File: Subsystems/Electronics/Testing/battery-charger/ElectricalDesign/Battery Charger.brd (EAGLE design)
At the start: 100 x 80 mm, 117 parts, among them J1 USB4515-GF-A_REVA, J3 10103592-0001LF, Q1 CSD16406Q3, Q2 CSD16406Q3, Q3 DMN2008LFU, Q4 DMN2008LFU, Q5 DMN2008LFU, Q6 BC817, Q7 BC817, SW6 [Override], U1 BQ24650, U2 BQ29700, U3 BQ29700, U4 BQ29700, U5 CP2102N-A02-GQFN28, U7 ESP32-S2-MINI-1

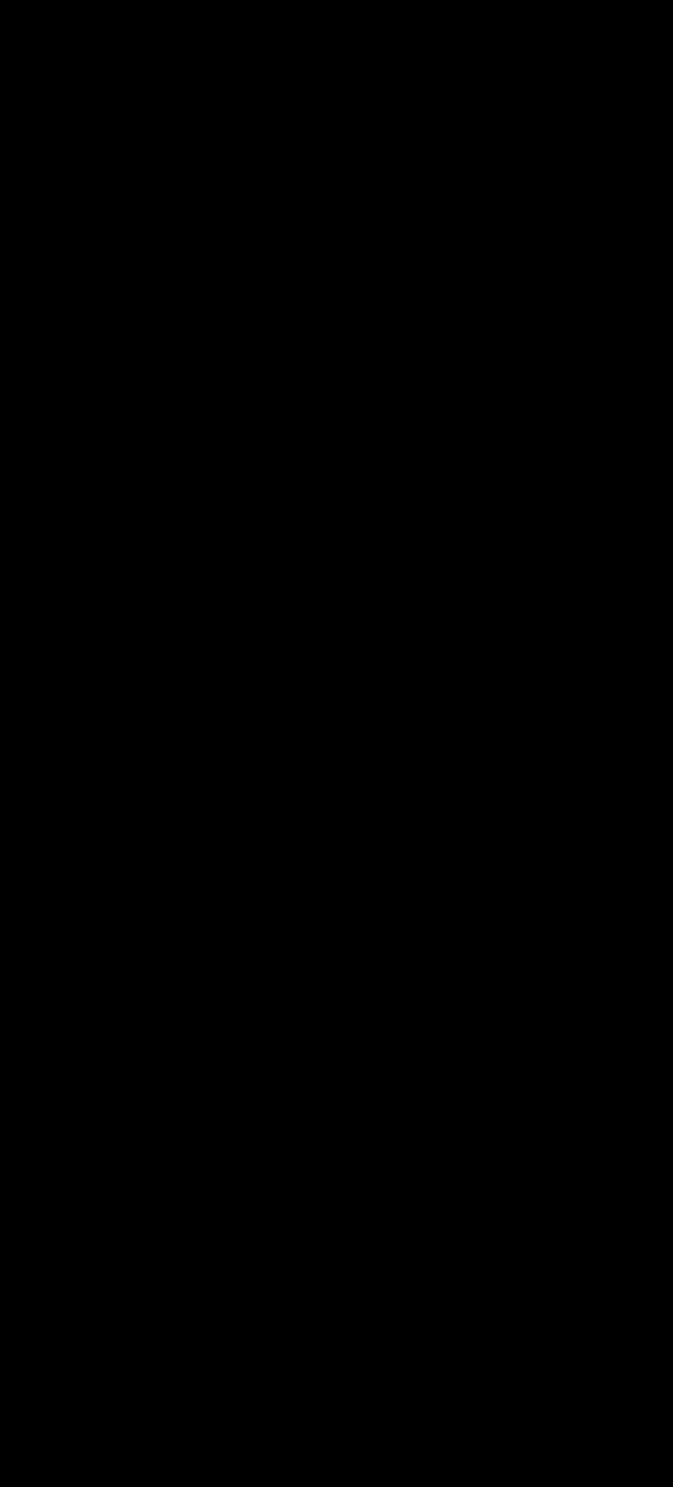
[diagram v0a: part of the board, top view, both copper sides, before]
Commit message: Added Test Points
Added test points for the important nets
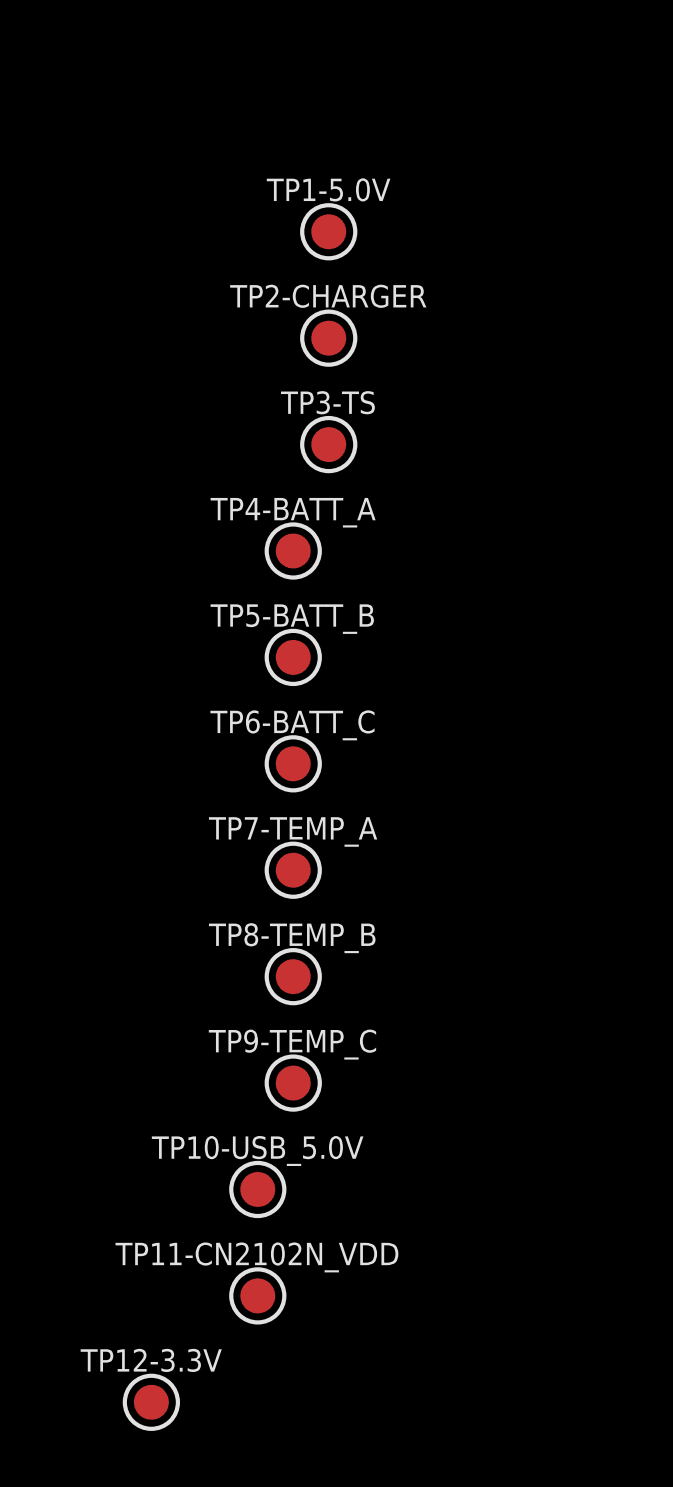
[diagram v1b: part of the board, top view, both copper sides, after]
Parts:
- added TP1-5.0V, TP10-USB_5.0V, TP11-CN2102N_VDD, TP12-3.3V, TP2-CHARGER, TP3-TS, TP4-BATT_A, TP5-BATT_B, TP6-BATT_C, TP7-TEMP_A, TP8-TEMP_B, TP9-TEMP_C: TEST_POINT-SMD-C-1.25, CougsInSpace-Connectors:SMD-C-1.25
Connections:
- removed net TEMP1: R38.1, RT1.2, U7.11
- removed net TEMP2: R39.1, RT2.2, U7.12
- removed net TEMP3: R40.1, RT3.2, U7.13
- new net TEMP_A: R38.1, RT1.2, TP7-TEMP_A.1, U7.11
- new net TEMP_B: R39.1, RT2.2, TP8-TEMP_B.1, U7.12
- new net TEMP_C: R40.1, RT3.2, TP9-TEMP_C.1, U7.13
- net 3.3V: now also TP12-3.3V.1
- net 5.0V: now also TP1-5.0V.1
- net CHARGER: now also TP2-CHARGER.1
- net CP2102N_VDD: now also TP11-CN2102N_VDD.1
- net D3_OUT: now also TP4-BATT_A.1
- net D4_OUT: now also TP5-BATT_B.1
- net D5_OUT: now also TP6-BATT_C.1
- net TS-ESP: now also TP3-TS.1
- net USB_VDD: now also TP10-USB_5.0V.1

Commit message: Completed Board Layout
Completed board layout, ready for review. Sense resistors were adjusted from 20m to 25m Ohm. Additional sense pins added.
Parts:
- added R42, R43: 0Ω <20mΩ, CougsInSpace-Resistors:1608
- added TP13-GND, TP14-D1_OUT: TEST_POINT-SMD-C-1.25, CougsInSpace-Connectors:SMD-C-1.25
- C20: value 10µF 10% -> 1µF 10%
- JP1: device pinhead:1X07 -> pinhead:1X11
- R18, R19: value 10mΩ 1% -> 50mΩ 1%; device CougsInSpace-Resistors:3216 -> CougsInSpace-Resistors:1608
- moved TP4-BATT_A 734.8 mm to (88.5, 70.5)
- moved TP7-TEMP_A 732.4 mm to (88.5, 56.5), turned to 180 degrees
- moved TP11-CN2102N_VDD 730.2 mm to (12.5, 61.5)
- moved TP12-3.3V 718.3 mm to (31.0, 39.5), turned to 90 degrees
- moved TP5-BATT_B 714.9 mm to (88.5, 45.5)
- moved TP10-USB_5.0V 713.4 mm to (10.5, 48.5), turned to 180 degrees
- moved TP8-TEMP_B 712.5 mm to (88.5, 31.5), turned to 180 degrees
- moved TP6-BATT_C 695.6 mm to (88.5, 21.0)
- moved TP9-TEMP_C 693.2 mm to (88.5, 7.00), turned to 180 degrees
- moved TP3-TS 686.4 mm to (53.5, 35.5)
- moved TP2-CHARGER 679.3 mm to (48.5, 33.5)
- moved TP1-5.0V 669.6 mm to (11.5, 38.0)
- moved R41 646.5 mm to (64.5, 50.5)
- moved C23 636.4 mm to (81.0, 65.0)
- moved C24 626.7 mm to (81.0, 40.0)
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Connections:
- removed net N$8: R18.2, R19.1
- new net CHASSIS: J1.S1, J1.S2, J1.S3, J1.S4, J3.S1, J3.S2, J3.S3, J3.S4, J3.S5, J3.S6, R43.1
- new net DGND: C25.2, C26.2, C27.2, C28.2, J3.5, R42.1, U5.29, U5.3
- net 3.3V: now also JP1.11
- net 5.0V: now also JP1.1
- net BQ24650_SR_P: now also R19.1
- net CHARGER: now also R18.2
- net D1_OUT: now also TP14-D1_OUT.1
- net ESP32_IO12: now also JP1.9; no longer JP1.7
- net ESP32_IO13: now also JP1.8; no longer JP1.6
- net ESP32_IO14: now also JP1.7; no longer JP1.5
- net ESP32_IO15: now also JP1.6; no longer JP1.4
- net ESP32_IO16: now also JP1.5; no longer JP1.3
- net ESP32_IO17: now also JP1.4; no longer JP1.2
- net ESP32_IO18: now also JP1.3; no longer JP1.1
- net PGND: now also JP1.10, JP1.2, R42.2, R43.2, TP13-GND.1; no longer C25.2, C26.2, C27.2, C28.2, J1.S1, J1.S2, J1.S3, J1.S4, J3.5, J3.S1, J3.S2, J3.S3, J3.S4, J3.S5, J3.S6, U5.29, U5.3
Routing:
- net PGND: track 0.00 -> 771.8 mm, vias 0 -> 22
- net 5.0V: track 0.00 -> 315.4 mm, vias 0 -> 11
- net TEMP_C: track 0.00 -> 114.5 mm, vias 0 -> 3
- net TEMP_B: track 0.00 -> 95.3 mm, vias 0 -> 3
- net TEMP_A: track 0.00 -> 93.7 mm, vias 0 -> 3
- net BQ297002_VSS: track 0.00 -> 91.6 mm
- net BQ297001_VSS: track 0.00 -> 91.6 mm
- net BQ297003_VSS: track 0.00 -> 91.3 mm
- net CHARGER: track 0.00 -> 81.0 mm
- net 3.3V: track 0.00 -> 75.5 mm, vias 0 -> 2
- net STAT3: track 0.00 -> 65.2 mm, vias 0 -> 3
- net STAT2: track 0.00 -> 60.5 mm, vias 0 -> 3
- net SW3: track 0.00 -> 54.8 mm, vias 0 -> 1
- net CHASSIS: track 0.00 -> 50.8 mm
- net D3_OUT: track 0.00 -> 50.3 mm
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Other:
- board size 100 x 80 mm -> 165 x 75 mm
- board text added: "12"
- board text added: "13"
- board text added: "14"
- board text added: "15"
- board text added: "16"
- board text added: "17"
- board text added: "18"
- board text added: "19"
- board text added: "20"
- board text added: "21"
- board text added: "26"
- board text added: "33"
- board text added: "34"
- board text added: "35"
- board text added: "36"
- board text added: "37"
- board text added: "38"
- board text added: "39"
- board text added: "3V3"
- board text added: "40"
- board text added: "41"
- board text added: "42"
- board text added: "45"
- board text added: "46"
- board text added: "5V"
- board text added: "Battery Charger V1.0.0"
- board text added: "Charging"
- board text added: "Complete"
- board text added: "GND"
- board text added: "Power"
- board text added: "Prog Data"
- board text added: "RESET"
- board text added: "TP1"
- board text added: "TP10"
- board text added: "TP11"
- board text added: "TP12"
- board text added: "TP13"
- board text added: "TP14"
- board text added: "TP2"
- board text added: "TP3"
- board text added: "TP4"
- board text added: "TP5"
- board text added: "TP6"
- board text added: "TP7"
- board text added: "TP8"
- board text added: "TP9"

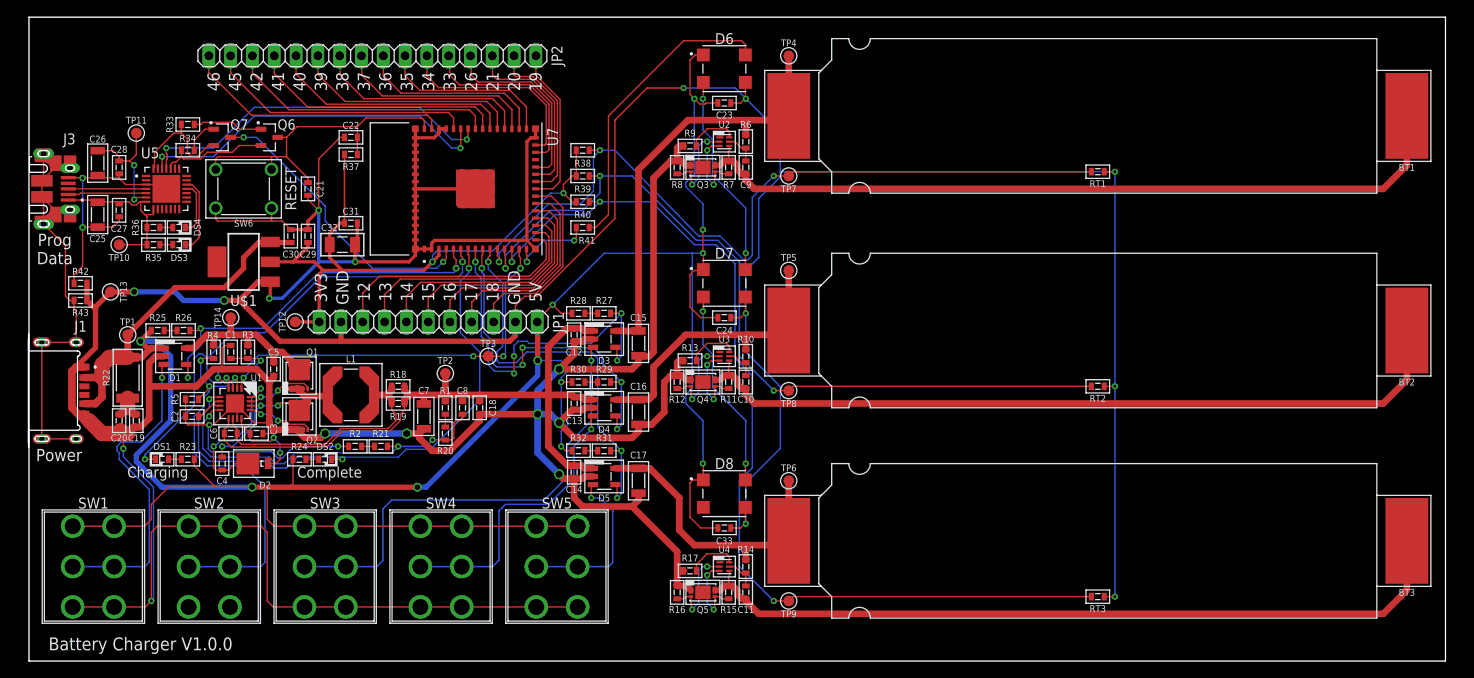
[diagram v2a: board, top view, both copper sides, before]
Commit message: Fixed Issues
Fixed some voltage level issues found while writing the documentation
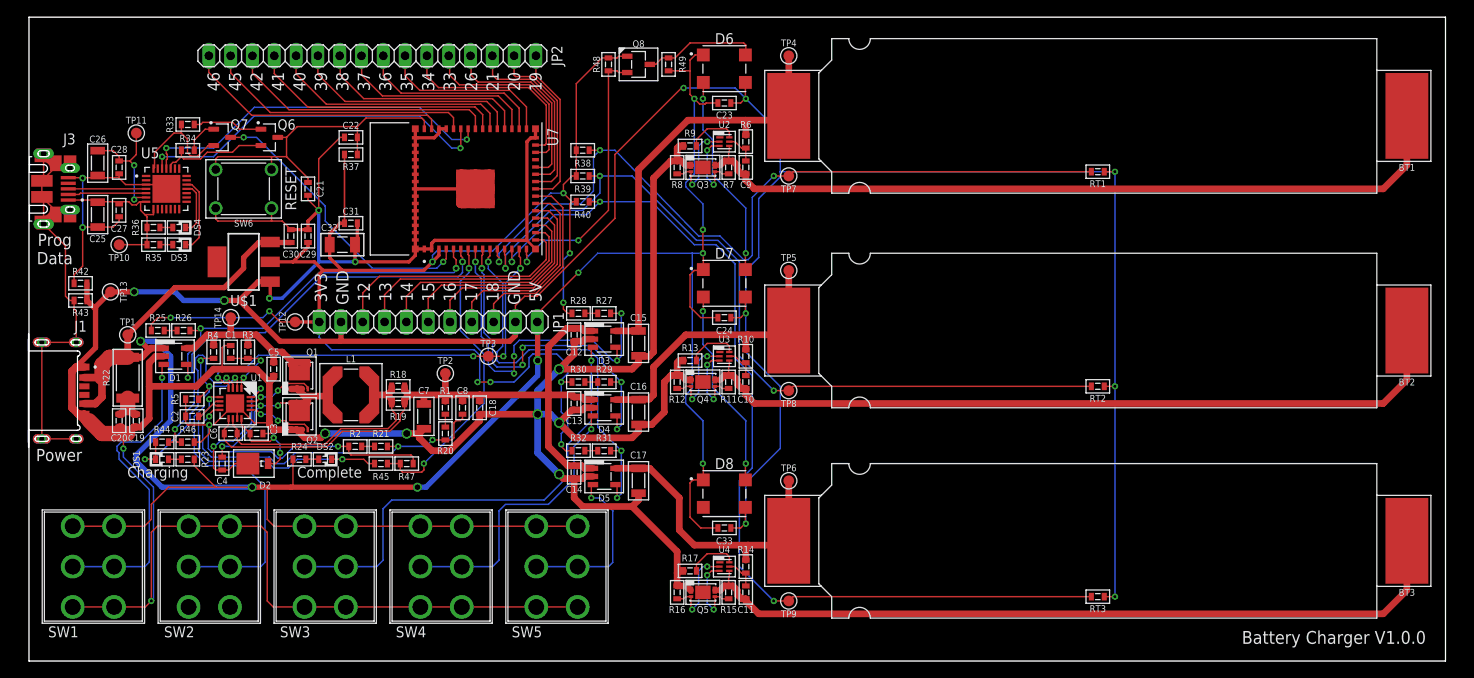
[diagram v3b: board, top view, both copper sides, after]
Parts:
- removed R41: 330Ω 1%, CougsInSpace-Resistors:1608
- added Q8: DMN53D0L, CougsInSpace-DiscreteSemi:SOT23-3
- added R44, R45: 75kΩ 0.1%, CougsInSpace-Resistors:1608
- added R46, R47: 100kΩ 0.1%, CougsInSpace-Resistors:1608
- added R48, R49: 10kΩ 0.1%, CougsInSpace-Resistors:1608
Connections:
- new net BQ24650_STAT1: DS1.C, R44.2, U1.3
- new net BQ24650_STAT2: DS2.C, R45.2, U1.5
- net 3.3V: now also Q8.1, R25.2, R28.2, R30.2, R32.2, R48.2
- net 5.0V: now also R49.2; no longer R25.2, R28.2, R30.2, R32.2
- net LED1_DIN: now also Q8.3, R49.1; no longer R41.2
- net LEDS: now also Q8.2, R48.1; no longer R41.1
- net PGND: now also R46.1, R47.1
- net STAT2: now also R44.1, R46.2; no longer DS1.C, U1.3
- net STAT3: now also R45.1, R47.2; no longer DS2.C, U1.5
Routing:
- net 3.3V: track 75.5 -> 174.0 mm, vias 2 -> 10
- net BQ24650_STAT2: track 0.00 -> 31.1 mm, vias 0 -> 2
- net STAT3: track 65.2 -> 35.5 mm, vias 3 -> 2
- net BQ24650_STAT1: track 0.00 -> 26.3 mm, vias 0 -> 2
- net LEDS: track 9.95 -> 32.3 mm
- net LED1_DIN: track 35.4 -> 13.5 mm
- net 5.0V: track 315.4 -> 297.2 mm, vias 11 -> 9
- net PGND: track 771.8 -> 781.8 mm
- net STAT2: track 60.5 -> 51.0 mm, vias 3 -> 2
- net STAT4: track 43.6 -> 42.6 mm
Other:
- board text added: "Batt A"
- board text added: "Batt B"
- board text added: "Batt C"
- board text added: "Enable"
- board text added: "Master"
- board text added: "ON"

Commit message: Added Signature
Added personal (Zachary) signature to library, schematic, and board. Also added LED color code text to physical board
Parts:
- added LOGO1: SIGNATUREZACHARY, CougsInSpace-Aesthetics:SIGN-ZACHARY
- renumbered TP11-CN2102N_VDD to TP11-CP2102N_VDD
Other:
- board text added: "Fault Waiting Charging Charged"
- board text added: "LED COLOR CODE:"
- board text added: "RED - YELLOW - BLUE - GREEN-"
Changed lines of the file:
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@@
 <text x="48" y="18.5" size="1.27" layer="27" font="vector" ratio="15" align="center">ON</text>
 <text x="61.5" y="18.5" size="1.27" layer="27" font="vector" ratio="15" align="center">ON</text>
+<text x="1.5" y="71.5" size="1.27" layer="51" font="vector" ratio="15" align="top-left">RED -
+YELLOW -
+BLUE -
+GREEN-</text>
+<text x="10.5" y="71.5" size="1.27" layer="51" font="vector" ratio="15" align="top-left">Fault
+Waiting
+Charging
+Charged</text>
+<text x="1.5" y="73.5" size="1.27" layer="51" font="vector" ratio="15" align="top-left">LED COLOR CODE:</text>
 </plain>
 <attributes>
@@
 <element name="TP9-TEMP_C" library="CougsInSpace-Connectors" package="SMD-C-1.25" value="TEST_POINT-SMD-C-1.25" x="88.5" y="7" smashed="yes" rot="R180"/>
 <element name="TP10-USB_5.0V" library="CougsInSpace-Connectors" package="SMD-C-1.25" value="TEST_POINT-SMD-C-1.25" x="10.5" y="48.5" smashed="yes" rot="R180"/>
-<element name="TP11-CN2102N_VDD" library="CougsInSpace-Connectors" package="SMD-C-1.25" value="TEST_POINT-SMD-C-1.25" x="12.5" y="61.5" smashed="yes"/>
+<element name="TP11-CP2102N_VDD" library="CougsInSpace-Connectors" package="SMD-C-1.25" value="TEST_POINT-SMD-C-1.25" x="12.5" y="61.5" smashed="yes"/>
 <element name="TP12-3.3V" library="CougsInSpace-Connectors" package="SMD-C-1.25" value="TEST_POINT-SMD-C-1.25" x="31" y="39.5" smashed="yes" rot="R90"/>
 <element name="R42" library="CougsInSpace-Resistors" package="1608" value="0Ω &lt;20mΩ" x="6" y="44" smashed="yes">
@@
 <attribute name="TEMP" value="25ppm/°C" x="74.5" y="69.5" size="1.778" layer="27" rot="R270" display="off"/>
 </element>
+<element name="LOGO1" library="CougsInSpace-Aesthetics" package="SIGN-ZACHARY" value="SIGNATUREZACHARY" x="55.5" y="23" smashed="yes"/>
 </elements>
 <signals>
@@
 <contactref element="C28" pad="1"/>
 <contactref element="C26" pad="1"/>
-<contactref element="TP11-CN2102N_VDD" pad="1"/>
+<contactref element="TP11-CP2102N_VDD" pad="1"/>
 <via x="12.25" y="53.75" extent="1-16" drill="0.35"/>
 <wire x1="12.5" y1="54" x2="12.25" y2="53.75" width="0.17" layer="1"/>
